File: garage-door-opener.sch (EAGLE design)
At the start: 19 parts, among them IC1 317T, K1 RR1A, T1 BC547, X1 Connector

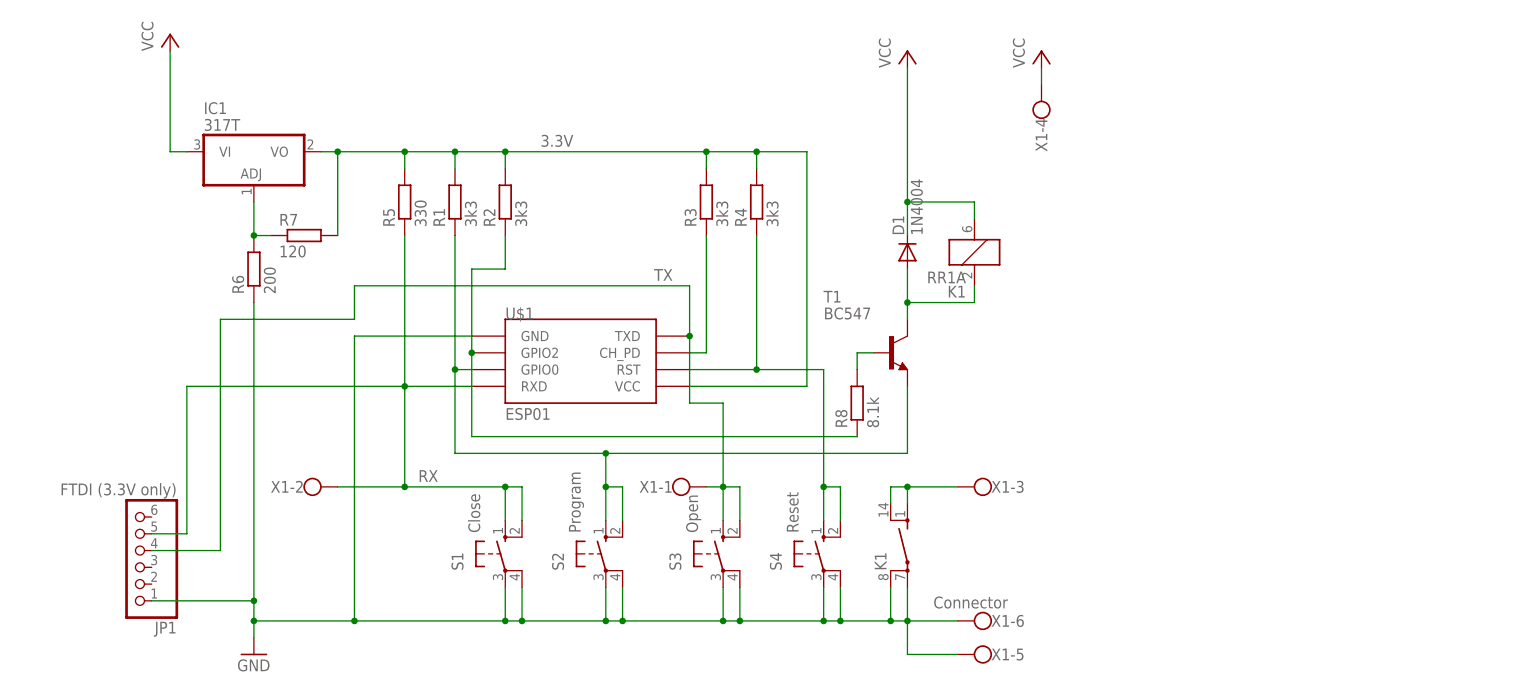
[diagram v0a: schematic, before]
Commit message: Rerouting board to use switch mode PSU, and removing development switches and pads. Need to use the pogoable version of the ESP12
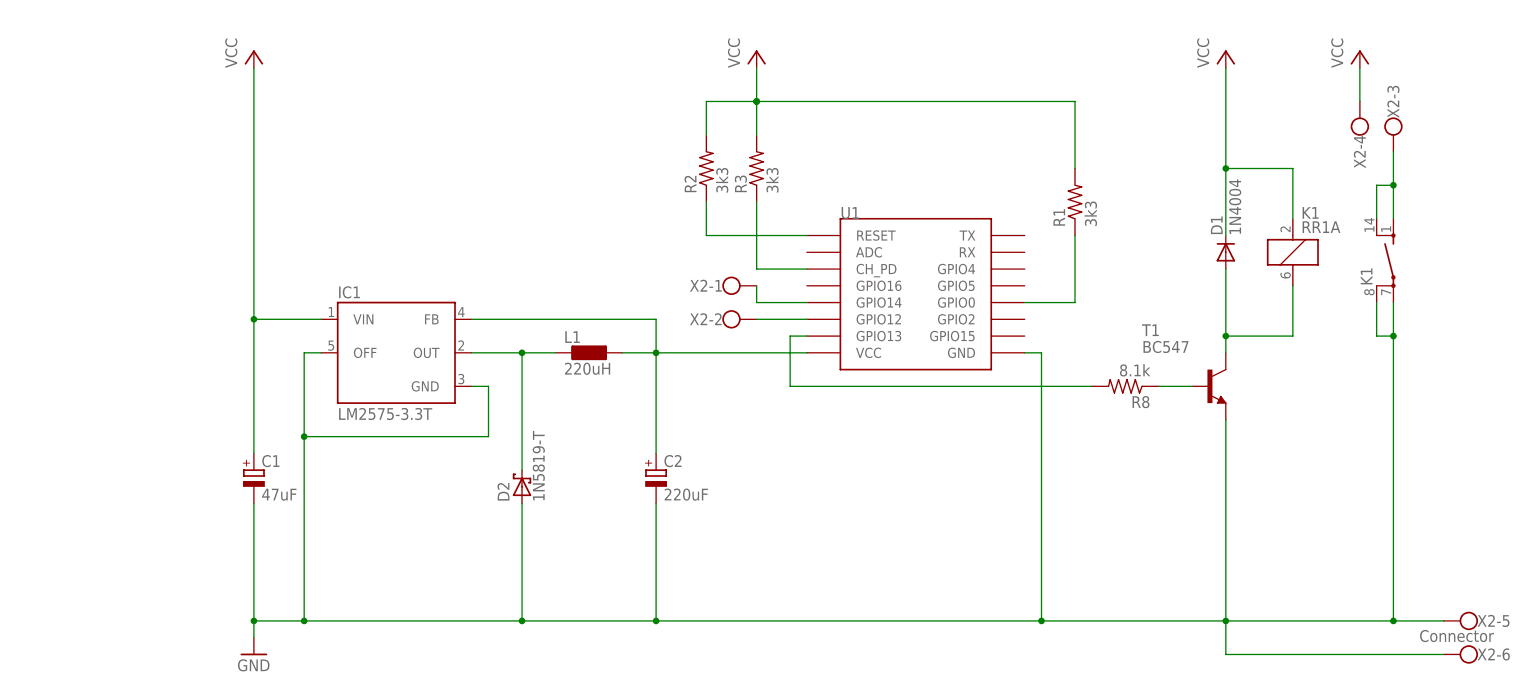
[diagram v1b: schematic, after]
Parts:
- removed JP1: FTDI (3.3V only), adafruit:PINHD-1X6
- removed R4: 3k3, resistor:R-EU_0204/7
- removed R5: 330, resistor:R-EU_0204/7
- removed R6: 200, resistor:R-EU_0204/7
- removed R7: 120, resistor:R-EU_0204/7
- removed S1: Close, switch-omron:10-XX
- removed S2: Program, switch-omron:10-XX
- removed S3: Open, switch-omron:10-XX
- removed S4: Reset, switch-omron:10-XX
- removed U$1: ESP01, esp8266modules:ESP01
- removed X1: Connector, con-wago-500:W237-6
- added C1: 47uF, rcl:CPOL-EUE5-4
- added C2: 220uF, rcl:CPOL-EUE5-8.5
- added D2: 1N5819-T, diode:1N5819-T
- added L1: 220uH, eagle-ltspice:L0207/10
- added U1: (no value), esp8266modules:ESP12SMD
- added X2: Connector, con-wago-500:W237-6
- IC1: value 317T -> LM2575-3.3T; device linear:317T -> lm2575:LM2575-3.3T
- R1, R2, R3, R8: device resistor:R-EU_0204/7 -> resistor:R-US_0207/10
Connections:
- removed net 3.3V: IC1.VO, R1.2, R2.2, R3.2, R4.2, R5.2, R7.2, U$1.VCC
- removed net RX: JP1.5, R5.1, S1.S, S1.S1, U$1.RXD, X1-2.KL
- removed net TX: JP1.4, S3.S, S3.S1, U$1.TXD, X1-1.KL
- new net N$11: U1.GPIO14, X2-1.KL
- new net N$4: C2.+, IC1.FB, L1.1, U1.VCC
- new net N$9: R8.2, U1.GPIO13
- net GND: now also C1.-, C2.-, D2.A, IC1.GND, IC1.OFF, T1.E, U1.GND, X2-5.KL, X2-6.KL; no longer JP1.1, R6.1, S1.P, S1.P1, S2.P, S2.P1, S3.P, S3.P1, S4.P, S4.P1, U$1.GND, X1-5.KL, X1-6.KL
- net N$1: now also K11.2; no longer K11.1
- net N$10: now also U1.GPIO12, X2-2.KL; no longer K12.S, K12.S@1, X1-3.KL
- net N$2: now also R8.1; no longer R8.2
- net N$3: now also D2.C, IC1.OUT, L1.2; no longer IC1.ADJ, R6.2, R7.1
- net N$5: now also K12.S, K12.S@1, X2-3.KL; no longer R1.1, S2.S, S2.S1, T1.E, U$1.GPIO0
- net N$6: now also R3.1, U1.CH_PD; no longer R2.1, R8.1, U$1.GPIO2
- net N$7: now also R1.1, U1.GPIO0; no longer R3.1, U$1.CH_PD
- net N$8: now also R2.1, U1.RESET; no longer R4.1, S4.S, S4.S1, U$1.RST
- net VCC: now also C1.+, IC1.VIN, K11.1, R1.2, R2.2, R3.2, X2-4.KL; no longer IC1.VI, K11.2, X1-4.KL
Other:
- moved on the sheet: D1, K1, T1

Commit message: Adding pull up resistors for all inputs for boot, hardwiring CH_PD, adding a config button to turn on the config website
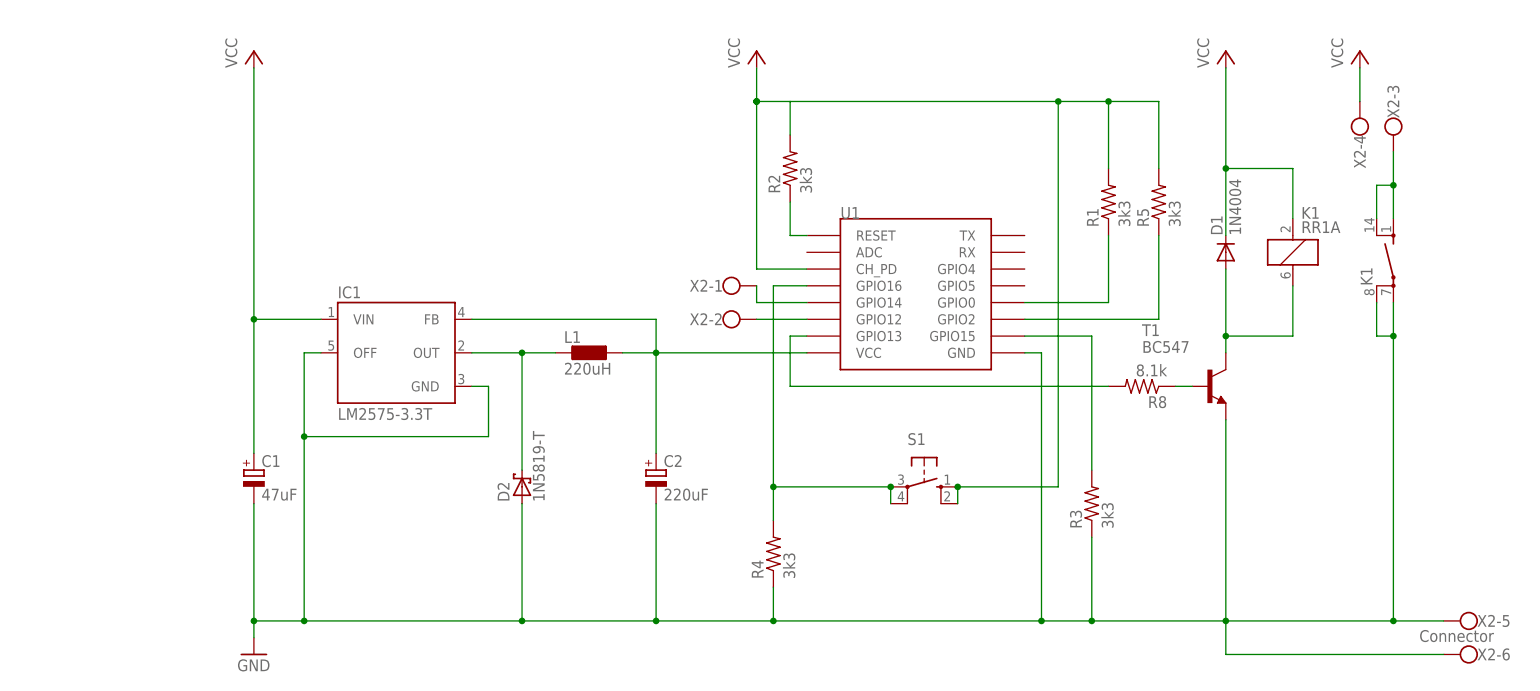
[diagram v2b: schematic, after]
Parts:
- added R4, R5: 3k3, resistor:R-US_0207/10
- added S1: (no value), switch-omron:10-XX
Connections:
- new net N$12: R4.2, S1.P, S1.P1, U1.GPIO16
- new net N$13: R5.1, U1.GPIO2
- net GND: now also R3.1, R4.1
- net N$6: now also R3.2, U1.GPIO15; no longer R3.1, U1.CH_PD
- net VCC: now also R5.2, S1.S, S1.S1, U1.CH_PD; no longer R3.2
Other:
- moved on the sheet: R1, R2, R3, R8
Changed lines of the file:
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@@
 <?xml version="1.0" encoding="utf-8"?>
 <!DOCTYPE eagle SYSTEM "eagle.dtd">
-<eagle version="8.7.1">
+<eagle version="8.6.0">
 <drawing>
 <settings>
@@
 <part name="K1" library="relay" library_urn="urn:adsk.eagle:library:339" deviceset="RR1A" device="" package3d_urn="urn:adsk.eagle:package:24316/1"/>
 <part name="X2" library="con-wago-500" library_urn="urn:adsk.eagle:library:195" deviceset="W237-6" device="" package3d_urn="urn:adsk.eagle:package:10696/1" value="Connector"/>
+<part name="S1" library="switch-omron" library_urn="urn:adsk.eagle:library:377" deviceset="10-XX" device="" package3d_urn="urn:adsk.eagle:package:27496/1"/>
+<part name="R4" library="resistor" library_urn="urn:adsk.eagle:library:348" deviceset="R-US_" device="0207/10" package3d_urn="urn:adsk.eagle:package:25939/1" value="3k3"/>
+<part name="R5" library="resistor" library_urn="urn:adsk.eagle:library:348" deviceset="R-US_" device="0207/10" package3d_urn="urn:adsk.eagle:package:25939/1" value="3k3"/>
 </parts>
 <sheets>
@@
 <instance part="D1" gate="1" x="152.4" y="60.96" rot="R90"/>
 <instance part="T1" gate="G$1" x="149.86" y="40.64"/>
-<instance part="R8" gate="G$1" x="137.16" y="40.64" rot="R180"/>
+<instance part="R8" gate="G$1" x="139.7" y="40.64" rot="R180"/>
 <instance part="GND2" gate="1" x="5.08" y="0"/>
 <instance part="P+2" gate="VCC" x="5.08" y="91.44"/>
@@
 <instance part="L1" gate="G$1" x="55.88" y="45.72" rot="R270"/>
 <instance part="P+4" gate="VCC" x="81.28" y="91.44"/>
-<instance part="R1" gate="G$1" x="129.54" y="68.58" rot="R90"/>
-<instance part="R2" gate="G$1" x="73.66" y="73.66" rot="R90"/>
-<instance part="R3" gate="G$1" x="81.28" y="73.66" rot="R90"/>
+<instance part="R1" gate="G$1" x="134.62" y="68.58" rot="R90"/>
+<instance part="R2" gate="G$1" x="86.36" y="73.66" rot="R90"/>
+<instance part="R3" gate="G$1" x="132.08" y="22.86" rot="R90"/>
 <instance part="K1" gate="1" x="162.56" y="60.96"/>
 <instance part="K1" gate="2" x="177.8" y="60.96"/>
@@
 <instance part="X2" gate="-5" x="190.5" y="5.08" rot="R180"/>
 <instance part="X2" gate="-6" x="190.5" y="0" rot="R180"/>
+<instance part="S1" gate="1" x="106.68" y="25.4" rot="R270"/>
+<instance part="R4" gate="G$1" x="83.82" y="15.24" rot="R90"/>
+<instance part="R5" gate="G$1" x="142.24" y="68.58" rot="R90"/>
 </instances>
 <busses>
@@
 <wire x1="12.7" y1="5.08" x2="45.72" y2="5.08" width="0.1524" layer="91"/>
 <wire x1="45.72" y1="5.08" x2="66.04" y2="5.08" width="0.1524" layer="91"/>
-<wire x1="66.04" y1="5.08" x2="124.46" y2="5.08" width="0.1524" layer="91"/>
-<wire x1="124.46" y1="5.08" x2="152.4" y2="5.08" width="0.1524" layer="91"/>
+<wire x1="66.04" y1="5.08" x2="83.82" y2="5.08" width="0.1524" layer="91"/>
+<wire x1="83.82" y1="5.08" x2="124.46" y2="5.08" width="0.1524" layer="91"/>
+<wire x1="124.46" y1="5.08" x2="132.08" y2="5.08" width="0.1524" layer="91"/>
+<wire x1="132.08" y1="5.08" x2="152.4" y2="5.08" width="0.1524" layer="91"/>
 <wire x1="152.4" y1="5.08" x2="177.8" y2="5.08" width="0.1524" layer="91"/>
 <junction x="152.4" y="5.08"/>
@@
 <wire x1="177.8" y1="48.26" x2="177.8" y2="5.08" width="0.1524" layer="91"/>
 <junction x="177.8" y="5.08"/>
+<pinref part="R4" gate="G$1" pin="1"/>
+<wire x1="83.82" y1="10.16" x2="83.82" y2="5.08" width="0.1524" layer="91"/>
+<junction x="83.82" y="5.08"/>
+<pinref part="R3" gate="G$1" pin="1"/>
+<wire x1="132.08" y1="17.78" x2="132.08" y2="5.08" width="0.1524" layer="91"/>
+<junction x="132.08" y="5.08"/>
 </segment>
 </net>
@@
 <segment>
 <pinref part="R2" gate="G$1" pin="2"/>
-<wire x1="73.66" y1="78.74" x2="73.66" y2="83.82" width="0.1524" layer="91"/>
-<wire x1="73.66" y1="83.82" x2="81.28" y2="83.82" width="0.1524" layer="91"/>
+<wire x1="86.36" y1="78.74" x2="86.36" y2="83.82" width="0.1524" layer="91"/>
 <pinref part="R1" gate="G$1" pin="2"/>
-<wire x1="81.28" y1="83.82" x2="129.54" y2="83.82" width="0.1524" layer="91"/>
-<wire x1="129.54" y1="83.82" x2="129.54" y2="73.66" width="0.1524" layer="91"/>
-<pinref part="R3" gate="G$1" pin="2"/>
-<wire x1="81.28" y1="78.74" x2="81.28" y2="83.82" width="0.1524" layer="91"/>
+<wire x1="81.28" y1="83.82" x2="86.36" y2="83.82" width="0.1524" layer="91"/>
+<wire x1="86.36" y1="83.82" x2="127" y2="83.82" width="0.1524" layer="91"/>
+<wire x1="127" y1="83.82" x2="134.62" y2="83.82" width="0.1524" layer="91"/>
+<wire x1="134.62" y1="83.82" x2="134.62" y2="73.66" width="0.1524" layer="91"/>
 <junction x="81.28" y="83.82"/>
 <pinref part="P+4" gate="VCC" pin="VCC"/>
 <wire x1="81.28" y1="88.9" x2="81.28" y2="83.82" width="0.1524" layer="91"/>
 <junction x="81.28" y="83.82"/>
+<pinref part="S1" gate="1" pin="S"/>
+<wire x1="111.76" y1="25.4" x2="127" y2="25.4" width="0.1524" layer="91"/>
+<wire x1="127" y1="25.4" x2="127" y2="83.82" width="0.1524" layer="91"/>
+<junction x="127" y="83.82"/>
+<pinref part="S1" gate="1" pin="S1"/>
+<wire x1="111.76" y1="22.86" x2="111.76" y2="25.4" width="0.1524" layer="91"/>
+<junction x="111.76" y="25.4"/>
+<pinref part="U1" gate="G$1" pin="CH_PD"/>
+<wire x1="88.9" y1="58.42" x2="81.28" y2="58.42" width="0.1524" layer="91"/>
+<wire x1="81.28" y1="58.42" x2="81.28" y2="83.82" width="0.1524" layer="91"/>
+<pinref part="R5" gate="G$1" pin="2"/>
+<wire x1="142.24" y1="73.66" x2="142.24" y2="83.82" width="0.1524" layer="91"/>
+<wire x1="142.24" y1="83.82" x2="134.62" y2="83.82" width="0.1524" layer="91"/>
+<junction x="134.62" y="83.82"/>
 </segment>
 </net>
@@
 <pinref part="R8" gate="G$1" pin="1"/>
 <pinref part="T1" gate="G$1" pin="B"/>
-<wire x1="142.24" y1="40.64" x2="147.32" y2="40.64" width="0.1524" layer="91"/>
-</segment>
-</net>
-<net name="N$6" class="0">
-<segment>
-<pinref part="U1" gate="G$1" pin="CH_PD"/>
-<wire x1="88.9" y1="58.42" x2="81.28" y2="58.42" width="0.1524" layer="91"/>
-<pinref part="R3" gate="G$1" pin="1"/>
-<wire x1="81.28" y1="68.58" x2="81.28" y2="58.42" width="0.1524" layer="91"/>
+<wire x1="144.78" y1="40.64" x2="147.32" y2="40.64" width="0.1524" layer="91"/>
 </segment>
 </net>
@@
 <segment>
 <pinref part="U1" gate="G$1" pin="GPIO0"/>
-<wire x1="121.92" y1="53.34" x2="129.54" y2="53.34" width="0.1524" layer="91"/>
+<wire x1="121.92" y1="53.34" x2="134.62" y2="53.34" width="0.1524" layer="91"/>
 <pinref part="R1" gate="G$1" pin="1"/>
-<wire x1="129.54" y1="53.34" x2="129.54" y2="63.5" width="0.1524" layer="91"/>
+<wire x1="134.62" y1="53.34" x2="134.62" y2="63.5" width="0.1524" layer="91"/>
 </segment>
 </net>
@@
 <segment>
 <pinref part="U1" gate="G$1" pin="RESET"/>
-<wire x1="88.9" y1="63.5" x2="73.66" y2="63.5" width="0.1524" layer="91"/>
+<wire x1="88.9" y1="63.5" x2="86.36" y2="63.5" width="0.1524" layer="91"/>
 <pinref part="R2" gate="G$1" pin="1"/>
-<wire x1="73.66" y1="63.5" x2="73.66" y2="68.58" width="0.1524" layer="91"/>
+<wire x1="86.36" y1="63.5" x2="86.36" y2="68.58" width="0.1524" layer="91"/>
 </segment>
 </net>
@@
 <pinref part="U1" gate="G$1" pin="GPIO13"/>
 <wire x1="88.9" y1="48.26" x2="86.36" y2="48.26" width="0.1524" layer="91"/>
-<wire x1="86.36" y1="40.64" x2="132.08" y2="40.64" width="0.1524" layer="91"/>
+<wire x1="86.36" y1="40.64" x2="134.62" y2="40.64" width="0.1524" layer="91"/>
 <pinref part="R8" gate="G$1" pin="2"/>
 <wire x1="86.36" y1="48.26" x2="86.36" y2="40.64" width="0.1524" layer="91"/>
@@
 </segment>
 </net>
+<net name="N$12" class="0">
+<segment>
+<pinref part="U1" gate="G$1" pin="GPIO16"/>
+<wire x1="88.9" y1="55.88" x2="83.82" y2="55.88" width="0.1524" layer="91"/>
+<pinref part="S1" gate="1" pin="P"/>
+<wire x1="83.82" y1="55.88" x2="83.82" y2="25.4" width="0.1524" layer="91"/>
+<wire x1="83.82" y1="25.4" x2="101.6" y2="25.4" width="0.1524" layer="91"/>
+<pinref part="S1" gate="1" pin="P1"/>
+<wire x1="101.6" y1="22.86" x2="101.6" y2="25.4" width="0.1524" layer="91"/>
+<junction x="101.6" y="25.4"/>
+<pinref part="R4" gate="G$1" pin="2"/>
+<wire x1="83.82" y1="25.4" x2="83.82" y2="20.32" width="0.1524" layer="91"/>
+<junction x="83.82" y="25.4"/>
+</segment>
+</net>
+<net name="N$6" class="0">
+<segment>
+<pinref part="U1" gate="G$1" pin="GPIO15"/>
+<pinref part="R3" gate="G$1" pin="2"/>
+<wire x1="121.92" y1="48.26" x2="132.08" y2="48.26" width="0.1524" layer="91"/>
+<wire x1="132.08" y1="48.26" x2="132.08" y2="27.94" width="0.1524" layer="91"/>
+</segment>
+</net>
+<net name="N$13" class="0">
+<segment>
+<pinref part="U1" gate="G$1" pin="GPIO2"/>
+<pinref part="R5" gate="G$1" pin="1"/>
+<wire x1="121.92" y1="50.8" x2="142.24" y2="50.8" width="0.1524" layer="91"/>
+<wire x1="142.24" y1="50.8" x2="142.24" y2="63.5" width="0.1524" layer="91"/>
+</segment>
+</net>
